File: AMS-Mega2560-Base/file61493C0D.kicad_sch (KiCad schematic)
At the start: 40 parts, among them IC10 OPA2340PA, IC7 LM2670SX-5.0_NOPB, IC8 LM2597MX-ADJ_NOPB, IC9 LM2597M-3.3_NOPB, J20 Screw_Terminal_01x02, J21 Conn_02x06_Odd_Even, Q4 IRF9Z34NPBF, U1 BK_HTC-15M, U2 TL431LP

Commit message: fixing some library settings and updating some schematics
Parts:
- R23, R24: footprint Resistor_THT:R_Axial_DIN0207_L6.3mm_D2.5mm_P5.08mm_Vertical -> Resistor_THT:R_Axial_DIN0207_L6.3mm_D2.5mm_P2.54mm_Vertical
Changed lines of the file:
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@@
       (effects (font (size 1.27 1.27)) (justify left))
     )
-    (property "Footprint" "Resistor_THT:R_Axial_DIN0207_L6.3mm_D2.5mm_P5.08mm_Vertical" (id 2) (at 275.082 41.91 90)
+    (property "Footprint" "Resistor_THT:R_Axial_DIN0207_L6.3mm_D2.5mm_P2.54mm_Vertical" (id 2) (at 275.082 41.91 90)
       (effects (font (size 1.27 1.27)) hide)
     )
@@
       (effects (font (size 1.27 1.27)) (justify left))
     )
-    (property "Footprint" "Resistor_THT:R_Axial_DIN0207_L6.3mm_D2.5mm_P5.08mm_Vertical" (id 2) (at 266.192 41.91 90)
+    (property "Footprint" "Resistor_THT:R_Axial_DIN0207_L6.3mm_D2.5mm_P2.54mm_Vertical" (id 2) (at 266.192 41.91 90)
       (effects (font (size 1.27 1.27)) hide)
     )

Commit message: BaseBoard fixes and updates. doing schematic work.
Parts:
- renumbered D1 to D6, D2 to D7, D3 to D8, IC8 to IC10, IC9 to IC11, IC10 to IC12, IC7 to IC9, J20 to J21, J21 to J22, Q4 to Q6, R14 to R21, R15 to R22, R16 to R23, R17 to R24, R18 to R25, R19 to R26, R20 to R27, R21 to R28, R22 to R29, R23 to R30, R24 to R31
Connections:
- net VoltageSensorOut renamed VoltageSensor

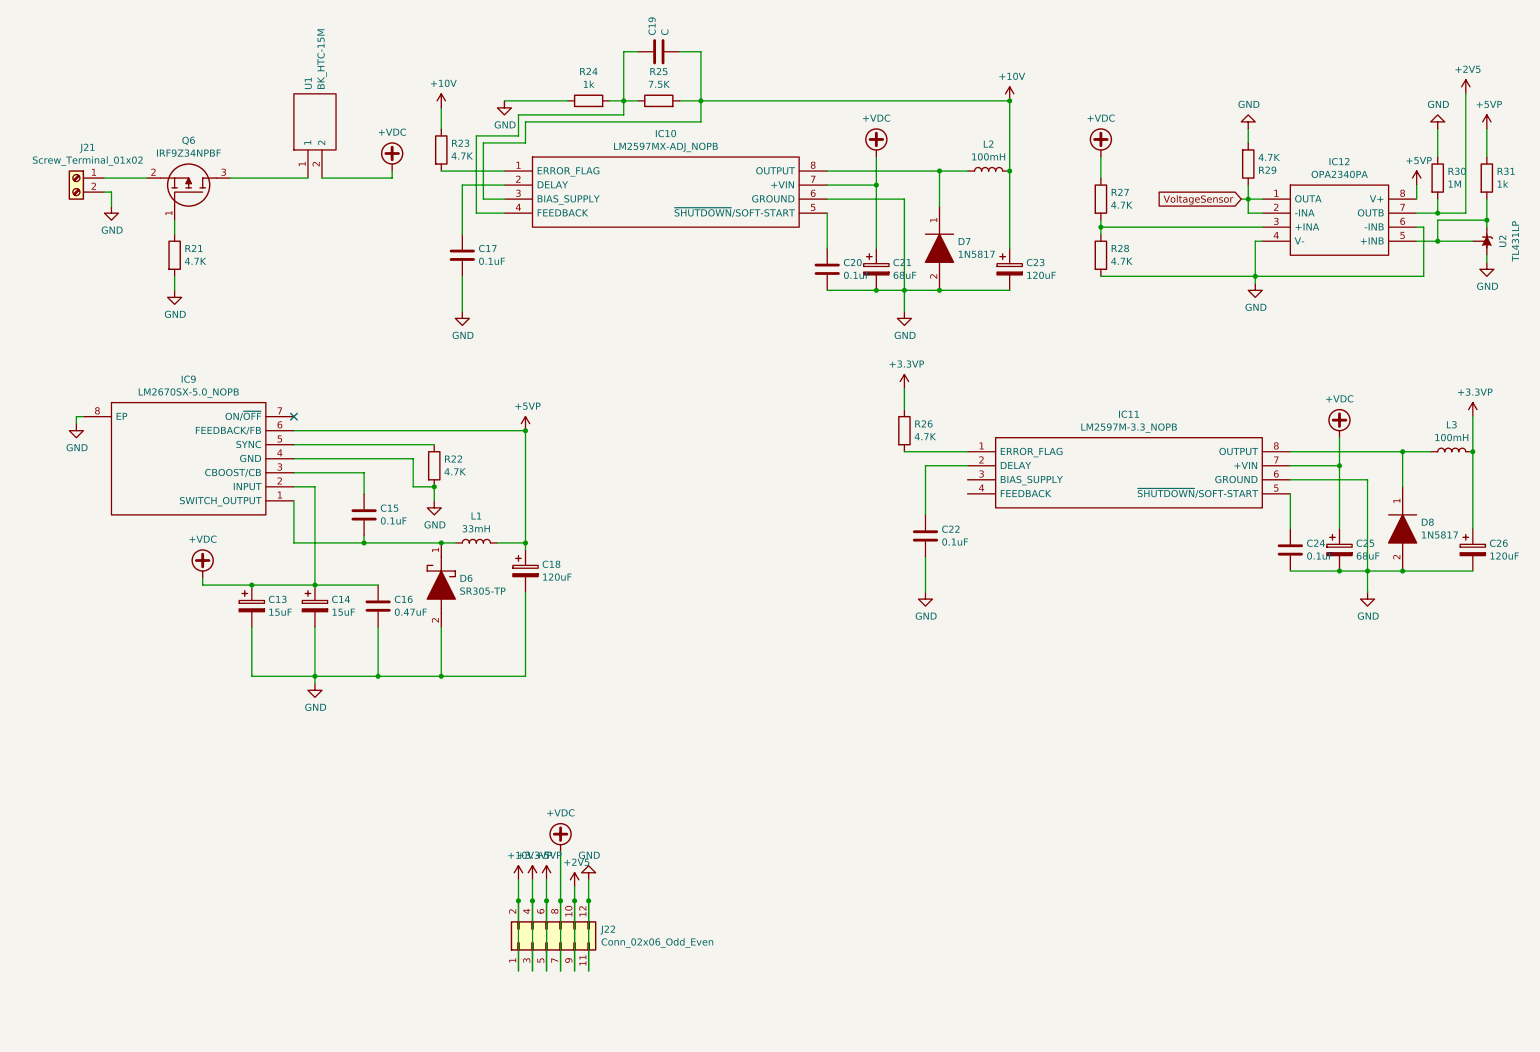
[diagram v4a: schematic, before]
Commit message: fixed the messed up references and cleaned up the schematic.
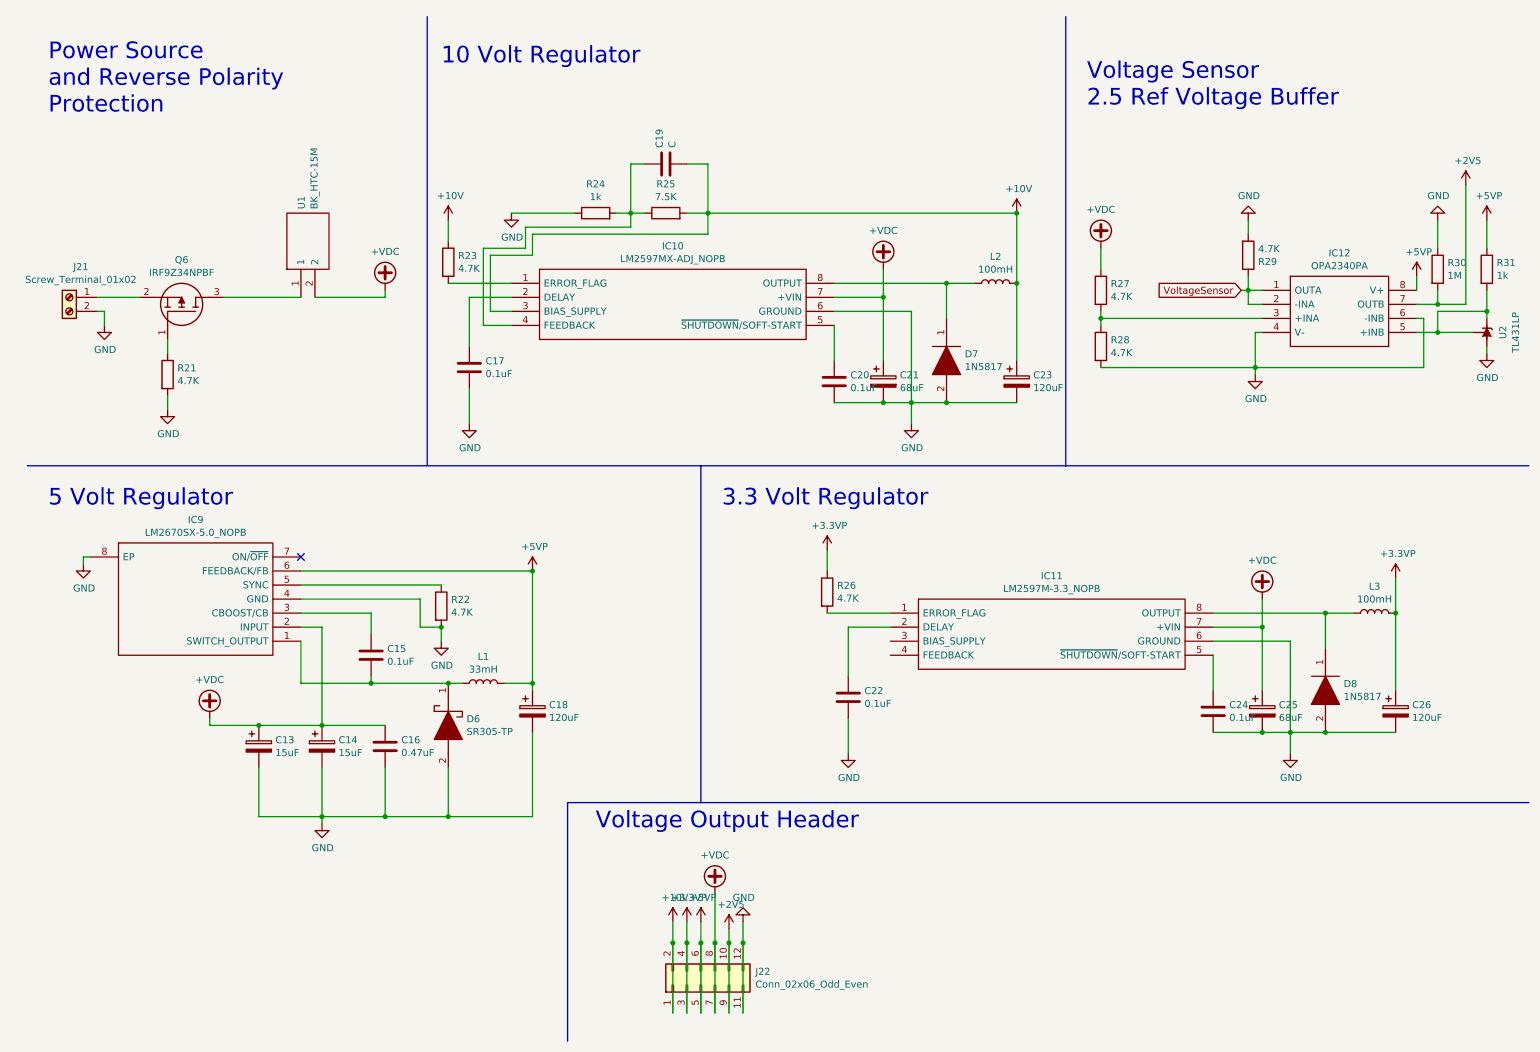
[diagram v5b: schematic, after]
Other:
- note added: "10 Volt Regulator"
- note added: "3.3 Volt Regulator"
- note added: "5 Volt Regulator"
- note added: "Power Source and Reverse Polarity Protection"
- note added: "Voltage Output Header"
- note added: "Voltage Sensor 2.5 Ref Voltage Buffer"
- moved on the sheet: C13, C14, C15, C16, C17, C18, C19, C20, C21, C22, C23, C24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

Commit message: working on pcb layout
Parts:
- removed J22: Conn_02x06_Odd_Even, Connector_PinSocket_2.54mm:PinSocket_2x06_P2.54mm_Vertical, symbol Connector_Generic:Conn_02x06_Odd_Even
- added J22: Conn_01x06, Connector_PinHeader_2.54mm:PinHeader_1x06_P2.54mm_Vertical, symbol Connector_Generic:Conn_01x06
- renumbered C22 to C21, C21 to C22
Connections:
- net +10V: now also J22.6 (Pin_6)
- net +2V5: now also J22.2 (Pin_2)
- net +3.3VP: now also J22.5 (Pin_5)
- net +5VP: now also J22.4 (Pin_4)
- net +VDC: now also J22.3 (Pin_3)
- net GND: now also J22.1 (Pin_1)

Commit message: wip for the base PCB, finished Vacuum PCB and Fab Files for that.
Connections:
- net +3.3VP: now also IC11.3 (BIAS_SUPPLY), IC11.4 (FEEDBACK)
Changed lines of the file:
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@@
   (junction (at 267.97 64.77) (diameter 0) (color 0 0 0 0)
   )
+  (junction (at 167.64 128.27) (diameter 0) (color 0 0 0 0)
+  )
   (junction (at 236.22 123.19) (diameter 0) (color 0 0 0 0)
   )
@@
   )
   (junction (at 241.3 142.24) (diameter 0) (color 0 0 0 0)
-  )
-  (junction (at 54.61 63.5) (diameter 0) (color 0 0 0 0)
   )
   (junction (at 27.94 63.5) (diameter 0) (color 0 0 0 0)
@@
     (stroke (width 0) (type default) (color 0 0 0 0))
   )
-  (wire (pts (xy 54.61 63.5) (xy 62.23 63.5))
-    (stroke (width 0) (type default) (color 0 0 0 0))
-  )
-  (wire (pts (xy 48.26 63.5) (xy 54.61 63.5))
+  (wire (pts (xy 48.26 63.5) (xy 62.23 63.5))
     (stroke (width 0) (type default) (color 0 0 0 0))
   )
@@
     (stroke (width 0) (type default) (color 0 0 0 0))
   )
+  (wire (pts (xy 167.64 128.27) (xy 168.91 128.27))
+    (stroke (width 0) (type default) (color 0 0 0 0))
+  )
   (wire (pts (xy 62.23 133.35) (xy 74.93 133.35))
     (stroke (width 0) (type default) (color 0 0 0 0))
@@
     (stroke (width 0) (type default) (color 0 0 0 0))
   )
+  (wire (pts (xy 168.91 125.73) (xy 167.64 125.73))
+    (stroke (width 0) (type default) (color 0 0 0 0))
+  )
   (wire (pts (xy 66.04 157.48) (xy 66.04 158.75))
     (stroke (width 0) (type default) (color 0 0 0 0))
@@
     (stroke (width 0) (type default) (color 0 0 0 0))
   )
+  (wire (pts (xy 167.64 125.73) (xy 167.64 128.27))
+    (stroke (width 0) (type default) (color 0 0 0 0))
+  )
   (wire (pts (xy 124.46 48.26) (xy 121.92 48.26))
     (stroke (width 0) (type default) (color 0 0 0 0))
@@
   )
   (wire (pts (xy 62.23 113.03) (xy 95.25 113.03))
+    (stroke (width 0) (type default) (color 0 0 0 0))
+  )
+  (wire (pts (xy 153.67 128.27) (xy 167.64 128.27))
     (stroke (width 0) (type default) (color 0 0 0 0))
   )
@@
     (pin "1")
   )
-  (symbol (lib_id "power:PWR_FLAG") (at 54.61 63.5 0) (unit 1)
-    (in_bom yes) (on_board yes) (fields_autoplaced)
-    (property "Reference" "#FLG04" (id 0) (at 54.61 61.595 0)
-      (effects (font (size 1.27 1.27)) hide)
-    )
-    (property "Value" "PWR_FLAG" (id 1) (at 54.61 59.8955 0))
-    (property "Footprint" "" (id 2) (at 54.61 63.5 0)
-      (effects (font (size 1.27 1.27)) hide)
-    )
-    (property "Datasheet" "~" (id 3) (at 54.61 63.5 0)
-      (effects (font (size 1.27 1.27)) hide)
-    )
-    (pin "1")
-  )
   (symbol (lib_id "Connector_Generic:Conn_01x06") (at 137.16 187.96 270) (unit 1)
     (in_bom yes) (on_board yes) (fields_autoplaced)
@@
     (pin "6")
   )
+  (symbol (lib_id "power:+3.3VP") (at 153.67 128.27 0) (unit 1)
+    (in_bom yes) (on_board yes)
+    (property "Reference" "#PWR0125" (id 0) (at 157.48 129.54 0)
+      (effects (font (size 1.27 1.27)) hide)
+    )
+    (property "Value" "+3.3VP" (id 1) (at 154.051 123.8758 0))
+    (property "Footprint" "" (id 2) (at 153.67 128.27 0)
+      (effects (font (size 1.27 1.27)) hide)
+    )
+    (property "Datasheet" "" (id 3) (at 153.67 128.27 0)
+      (effects (font (size 1.27 1.27)) hide)
+    )
+    (pin "1")
+  )
   (symbol (lib_id "power:PWR_FLAG") (at 95.25 113.03 0) (unit 1)
